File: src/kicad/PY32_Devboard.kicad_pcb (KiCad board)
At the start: 2 copper layers, 28.4 x 47.7 mm, 19 parts, among them J2 Micro_SD_Card, J5 Conn_01x09, J6 Conn_01x09, U1 CH340N, U2 ME6211A33M3G-N, U3 PY32F002BF15P6TR

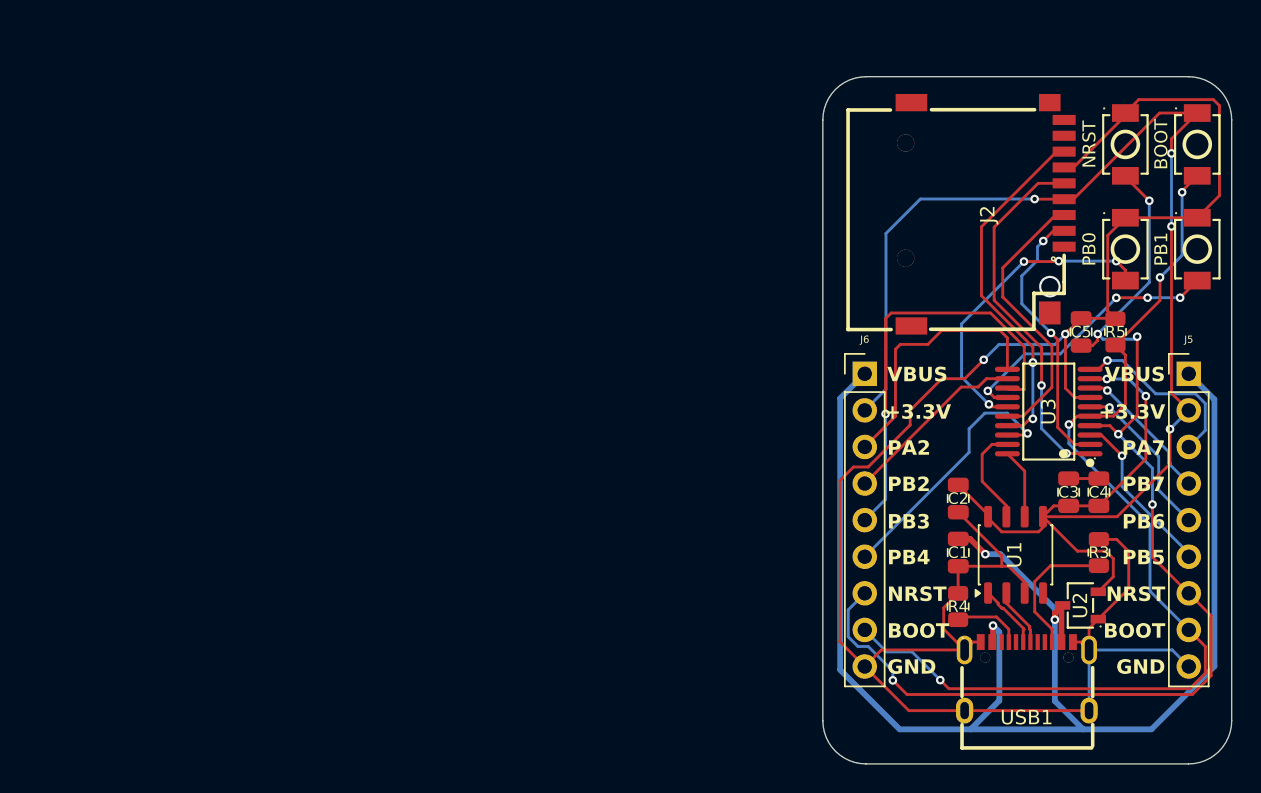
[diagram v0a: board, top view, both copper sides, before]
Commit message: Changed Github For Fixed PCB
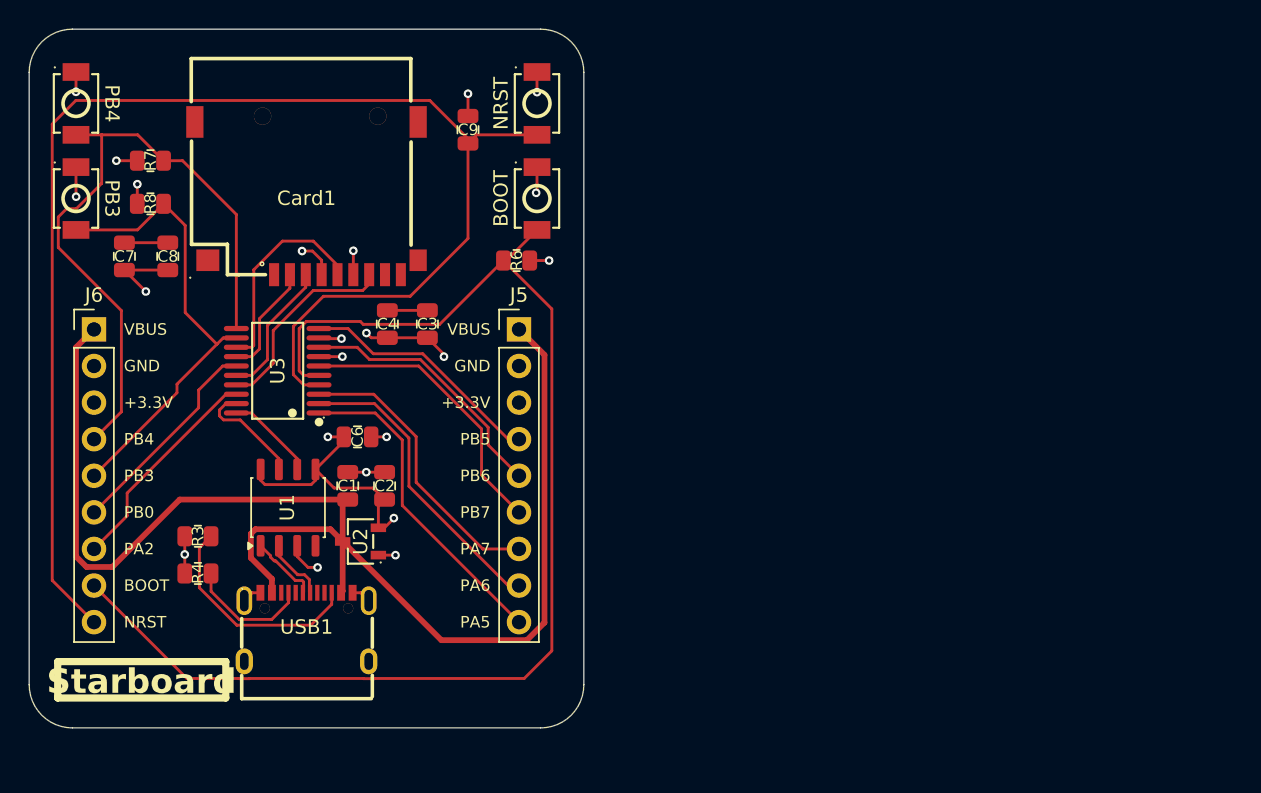
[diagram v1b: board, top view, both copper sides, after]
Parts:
- removed C5: 100nF, Capacitor_SMD:C_0805_2012Metric
- removed J2: Micro_SD_Card, easyeda2kicad:TF-SMD_TF-PUSH
- removed PB0: RESET, easyeda2kicad:SW-SMD_L3.9-W3.0-P4.45
- removed PB1: BOOT, easyeda2kicad:SW-SMD_L3.9-W3.0-P4.45
- removed R5: 10k, Resistor_SMD:R_0805_2012Metric
- added C6: 100nF, Capacitor_SMD:C_0805_2012Metric, F.Cu at (103.5, 86.8)
- added C7: 100nF, Capacitor_SMD:C_0805_2012Metric, F.Cu at (87.4, 74.3)
- added C8: 1uF, Capacitor_SMD:C_0805_2012Metric, F.Cu at (90.4, 74.3)
- added C9: 100nF, Capacitor_SMD:C_0805_2012Metric, F.Cu at (111.2, 65.5)
- added Card1: TF PUSH, easyeda2kicad:TF-SMD_TF-PUSH, F.Cu at (100.0, 70.2)
- added PB3: PB1, easyeda2kicad:SW-SMD_L3.9-W3.0-P4.45, F.Cu at (84.0, 70.3)
- added PB4: PB0, easyeda2kicad:SW-SMD_L3.9-W3.0-P4.45, F.Cu at (84.0, 63.7)
- added R6: 10k, Resistor_SMD:R_0805_2012Metric, F.Cu at (114.6, 74.6)
- added R7: 10k, Resistor_SMD:R_0805_2012Metric, F.Cu at (89.2, 67.6)
- added R8: 10k, Resistor_SMD:R_0805_2012Metric, F.Cu at (89.2, 70.6)
- moved R3 62.5 mm to (92.5, 93.7), turned to 180 degrees
- moved U3 53.6 mm to (98.0, 82.2)
- moved J6 53.6 mm to (85.2, 79.3)
- moved R4 52.8 mm to (92.5, 96.3), turned to 180 degrees
- moved C4 50.7 mm to (105.6, 79.0)
- moved U1 50.6 mm to (98.7, 91.7)
- moved U2 50.2 mm to (103.8, 94.1)
- moved USB1 50.1 mm to (100.0, 100.0)
- moved J5 46.6 mm to (114.8, 79.3)
- moved C3 46.0 mm to (108.4, 79.0)
- moved BOOT 46.0 mm to (116.0, 70.3)
- moved C1 42.6 mm to (102.9, 90.2), turned to 90 degrees
- moved NRST 40.9 mm to (116.0, 63.7)
- moved C2 39.8 mm to (105.4, 90.2), turned to 90 degrees
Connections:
- J5 pad 2: +3.3V -> GND
- J5 pad 3: /PB5 -> +3.3V
- J5 pad 4: /PB6 -> /PB5
- J5 pad 5: /PB7 -> /PB6
- J5 pad 6: /PA7 -> /PB7
- J5 pad 7: /NRST -> /PA7
- J5 pad 8: /BOOT -> /PA6
- J5 pad 9: GND -> /PA5
- J6 pad 2: +3.3V -> GND
- J6 pad 3: /PB4 -> +3.3V
- J6 pad 4: /PB3 -> /PB4
- J6 pad 5: /PB2 -> /PB3
- J6 pad 6: /PA2 -> /PB0
- J6 pad 7: /NRST -> /PA2
- J6 pad 9: GND -> /NRST
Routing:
- net GND: track 145.0 -> 23.6 mm, vias 2 -> 12
- net /PB4: track 18.4 -> 46.7 mm
- net /NRST: track 78.1 -> 98.5 mm, vias 6 -> 0
- net /PB3: track 12.9 -> 32.3 mm
- net /BOOT: track 70.0 -> 87.7 mm, vias 4 -> 0
- net +3.3V: track 109.1 -> 124.6 mm, vias 6 -> 10
- net /PB2: track 29.5 -> 14.5 mm, vias 1 -> 0
- net /PB1: track 19.3 -> 7.86 mm, vias 4 -> 0
- net /PA1: track 24.7 -> 14.1 mm, vias 2 -> 0
- net /PA0: track 19.4 -> 9.61 mm
- net VBUS: track 102.9 -> 94.0 mm, vias 3 -> 0
- net /PB7: track 11.5 -> 20.0 mm, vias 1 -> 0
- net /PA7: track 11.7 -> 20.2 mm, vias 1 -> 0
- net /PB6: track 10.1 -> 18.3 mm, vias 1 -> 0
- net /PB0: track 21.9 -> 14.8 mm, vias 4 -> 0
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- added copper zone on In1.Cu, net GND
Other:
- board size 28.4 x 47.7 mm -> 38.5 x 48.5 mm
- copper layers 2 -> 4
- board text added: "PA5"
- board text added: "PA6"
- board text added: "PB0"
- board text removed: "PB2"
